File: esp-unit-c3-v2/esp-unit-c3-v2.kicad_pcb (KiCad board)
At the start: 2 copper layers, 31.2 x 42 mm, 80 parts, among them J1 JST SH1.0, J2 JST PH2.0, J3 USB C 16P, Q1 DMG3415U, SW1 BOOT, SW2 RESET, SW3 MSK-12C02-07, U1 ESP32-C3-MINI-1, U2 Delta_Board-1, U3 MCP73831T-2ACI/OT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

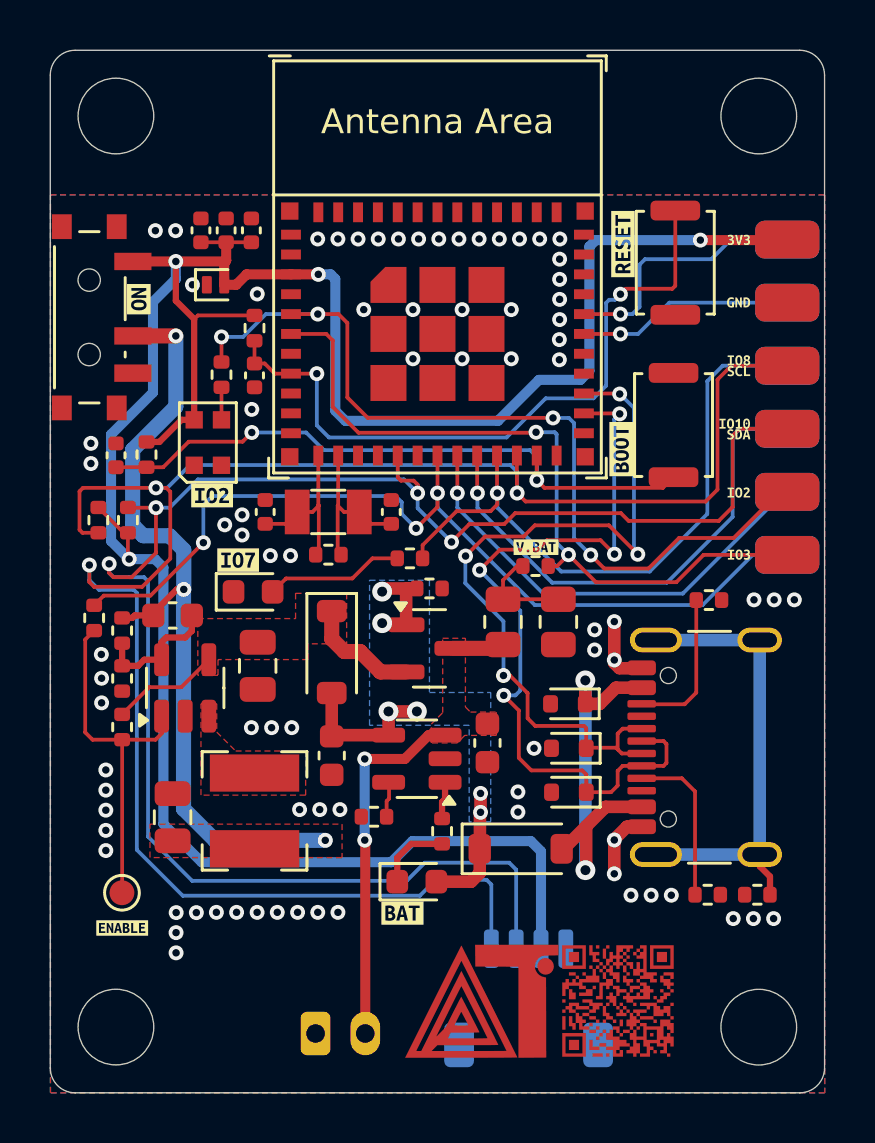
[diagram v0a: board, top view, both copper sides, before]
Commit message: add sensor board
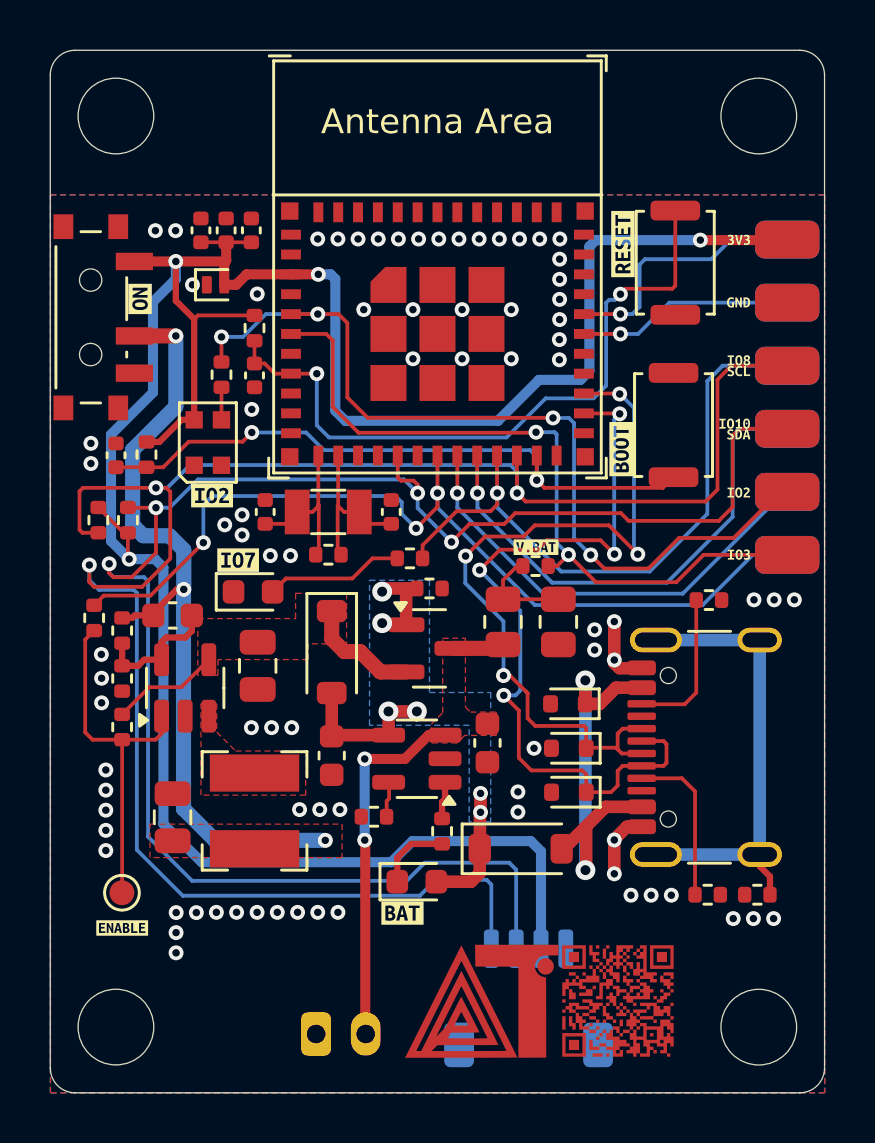
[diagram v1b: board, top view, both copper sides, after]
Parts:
- J2: footprint Connector_JST:JST_PH_S2B-PH-K_1x02_P2.00mm_Horizontal -> DeltaT32:JST_PH2.0
- SW3: footprint Button_Switch_SMD:SW_SPDT_PCM12 -> DeltaT32:MSK-12C02-07
- moved J2 2.90 mm to (122.3, 104.4)
- moved SW3 0.16 mm to (112.5, 78.2)
- moved kibuzzard-680CDAE0 0.05 mm to (114.2, 77.6)
